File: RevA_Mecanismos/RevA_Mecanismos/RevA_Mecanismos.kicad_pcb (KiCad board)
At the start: 4 copper layers, 99.7 x 99.7 mm, 137 parts, among them IC1 MAX33040EAKA+T, J1 Conn_01x02_Socket, J10 Screw_Terminal_01x02, J11 Screw_Terminal_01x02, J12 Conn_01x08_Socket, J13 Conn_01x08_Socket, J14 Conn_01x02_Pin, J15 430450624, J16 Conn_01x07_Pin, J17 Conn_01x02_Pin, J18 Conn_01x02_Pin, J19 Conn_01x02_Pin, J2 PROG, J20 3557-2, J21 Conn_01x04_Pin, J22 Conn_01x04_Pin, J3 Conn_01x02_Pin, J4 430450224, J5 430450224, J6 430450224, J7 430450224, J8 3557-2, J9 3557-2, Q1 FDN335N, Q2 NDS352AP, Q3 IRF9540NSPBF, Q4 IRF9540NSPBF, Q5 IRF9540NSPBF, Q6 IRF9540NSPBF, SW1 SW_Push, U1 STM32L431RCTx, U2 R-78E3.3-1.0, U3 R-78E5.0-1.0, U4 IRF540SPBF, U5 IRF540SPBF, U6 IRF540SPBF, U7 IRF540SPBF, U8 TXB0104D, Y1 16MHz

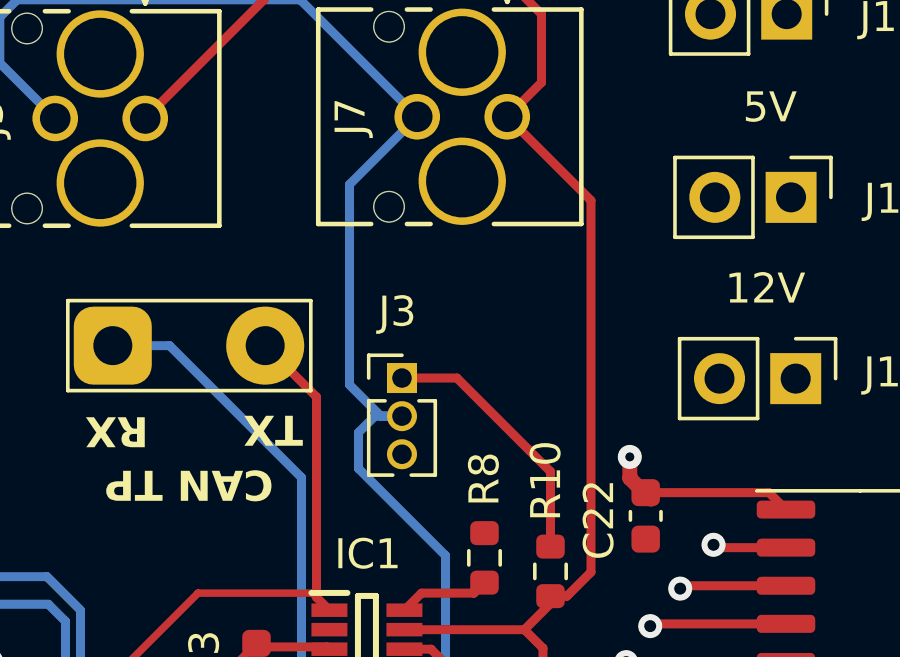
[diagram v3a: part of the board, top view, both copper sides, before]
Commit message: Correction made to footprint for J3 pin header
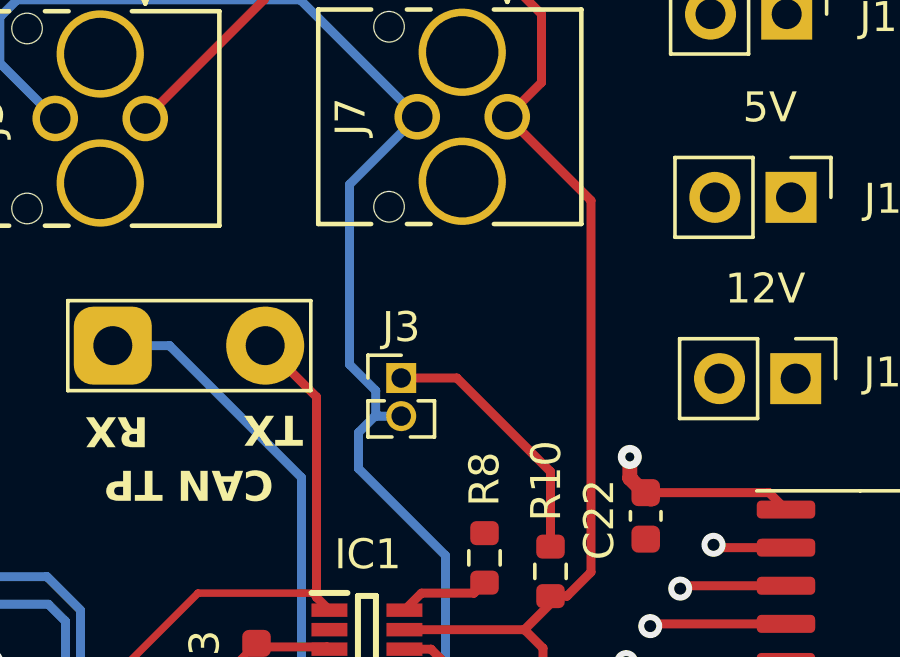
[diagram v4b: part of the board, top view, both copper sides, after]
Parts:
- J3: footprint Connector_PinHeader_1.27mm:PinHeader_1x03_P1.27mm_Vertical -> Connector_PinHeader_1.27mm:PinHeader_1x02_P1.27mm_Vertical
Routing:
- net CAN_N: track 136.3 -> 135.5 mm

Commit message: PCB Routing completed
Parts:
- moved C23 2.21 mm to (111.1, 74.0), turned to 0 degrees
- moved C1 1.47 mm to (85.3, 90.8)
- moved R24 1.21 mm to (130.8, 76.7)
- moved R39 1.21 mm to (130.9, 78.6)
- moved C18 1.20 mm to (120.2, 76.5)
- moved U4 1.12 mm to (156.6, 83.8)
- moved U6 1.12 mm to (144.7, 83.7)
- moved R31 0.97 mm to (136.9, 115.7)
- moved R34 0.95 mm to (137.0, 117.7)
- moved R33 0.85 mm to (137.5, 75.7)
- moved R28 0.85 mm to (137.5, 73.6)
- moved J20 0.76 mm to (115.1, 117.3)
- moved C10 0.63 mm to (80.3, 96.8)
- moved R37 0.50 mm to (130.6, 112.7)
- moved R26 0.50 mm to (130.5, 110.9)
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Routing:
- net +12V: track 26.7 -> 174.0 mm, vias 0 -> 1
- net +5V: track 23.5 -> 143.2 mm, vias 0 -> 3
- net WPM_TIM1_CH1: track 1.95 -> 120.8 mm, vias 0 -> 2
- net WP_TIM1_CH2N: track 0.00 -> 104.9 mm, vias 0 -> 2
- net STPR_STEP: track 0.00 -> 81.3 mm, vias 0 -> 4
- net WPM_TIM1_CH1N: track 0.00 -> 61.5 mm, vias 0 -> 2
- net Net-(Q4-S): track 16.4 -> 73.0 mm, vias 1 -> 4
- net Net-(Q3-S): track 28.4 -> 84.5 mm, vias 1 -> 6
- net Net-(U7-G): track 7.16 -> 62.6 mm, vias 0 -> 2
- net LEVEL_SHIFTER: track 0.00 -> 51.8 mm, vias 0 -> 2
- net STPR_DIR: track 32.2 -> 81.4 mm, vias 0 -> 2
- net WP_TIM1_CH2: track 0.00 -> 45.4 mm, vias 0 -> 2
- net WPM_+: track 18.4 -> 59.6 mm, vias 0 -> 1
- net +VMOT: track 107.8 -> 146.3 mm, vias 0 -> 2
- net STPR_EN: track 30.8 -> 63.0 mm
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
